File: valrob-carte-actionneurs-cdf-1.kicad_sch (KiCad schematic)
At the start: 57 parts, among them J10 Conn_01x04_Pin, J2 Conn_01x02, J3 USB_C_Receptacle_USB2.0_14P, J4 Conn_01x02, M1 Motor_Servo, U2 SN65HVD230, U3 LDL212PV33R, U5 ESP32-S3FN8, Y1 48M

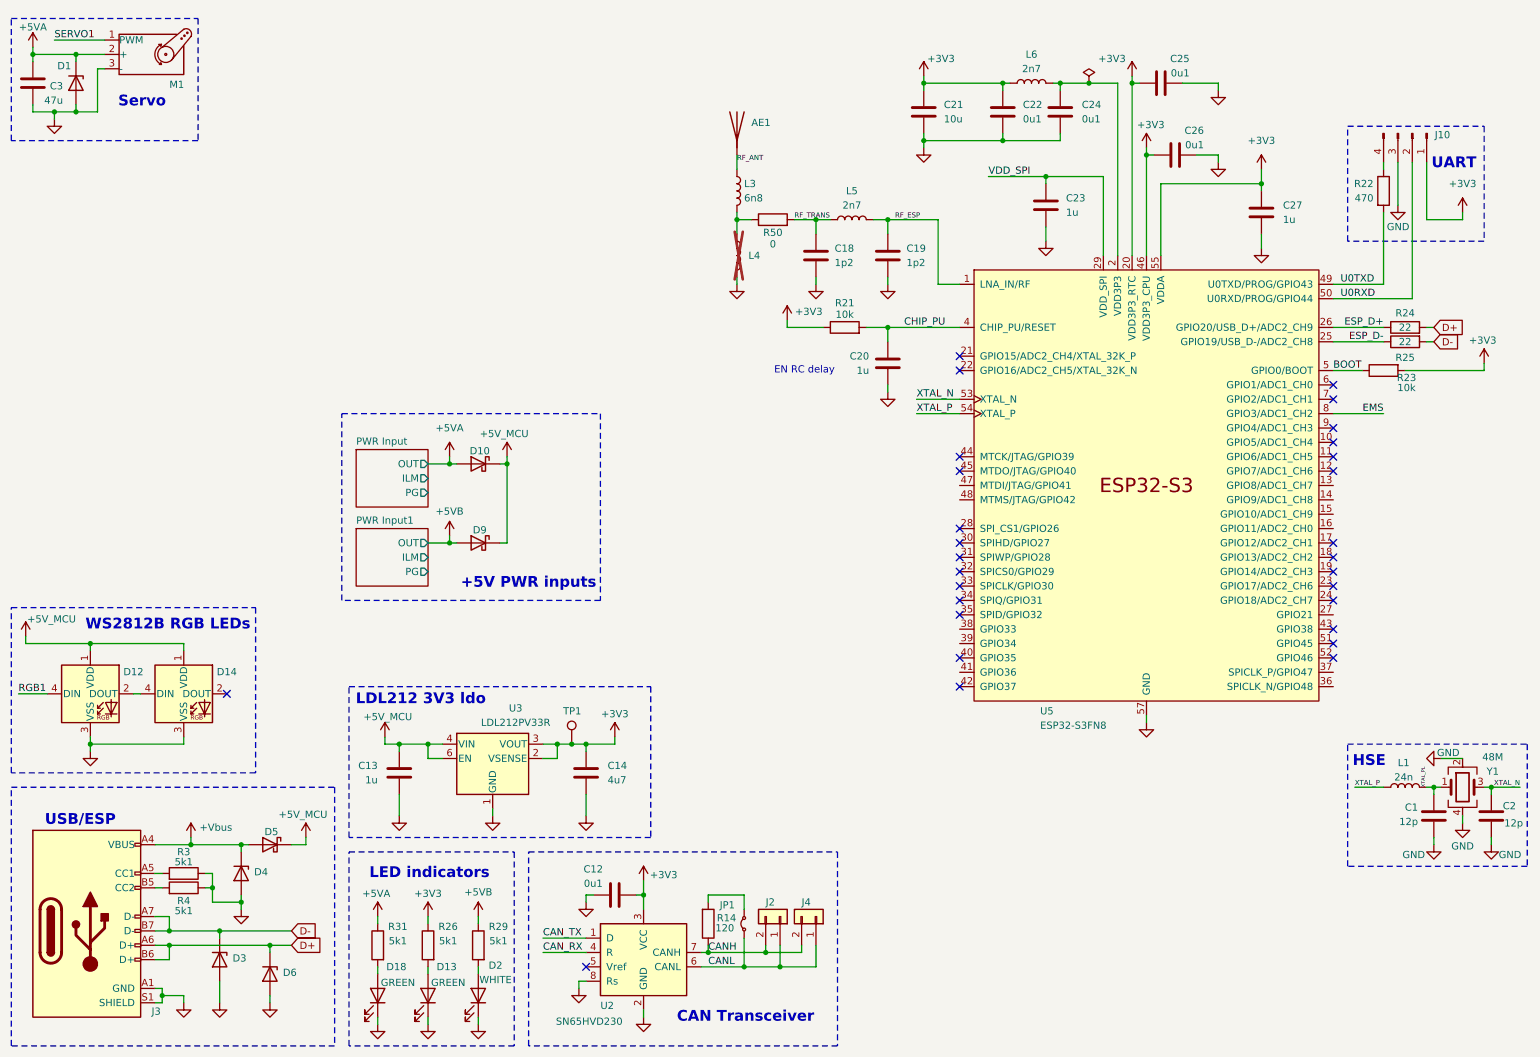
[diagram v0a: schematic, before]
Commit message: schem: connect peripherals gpios
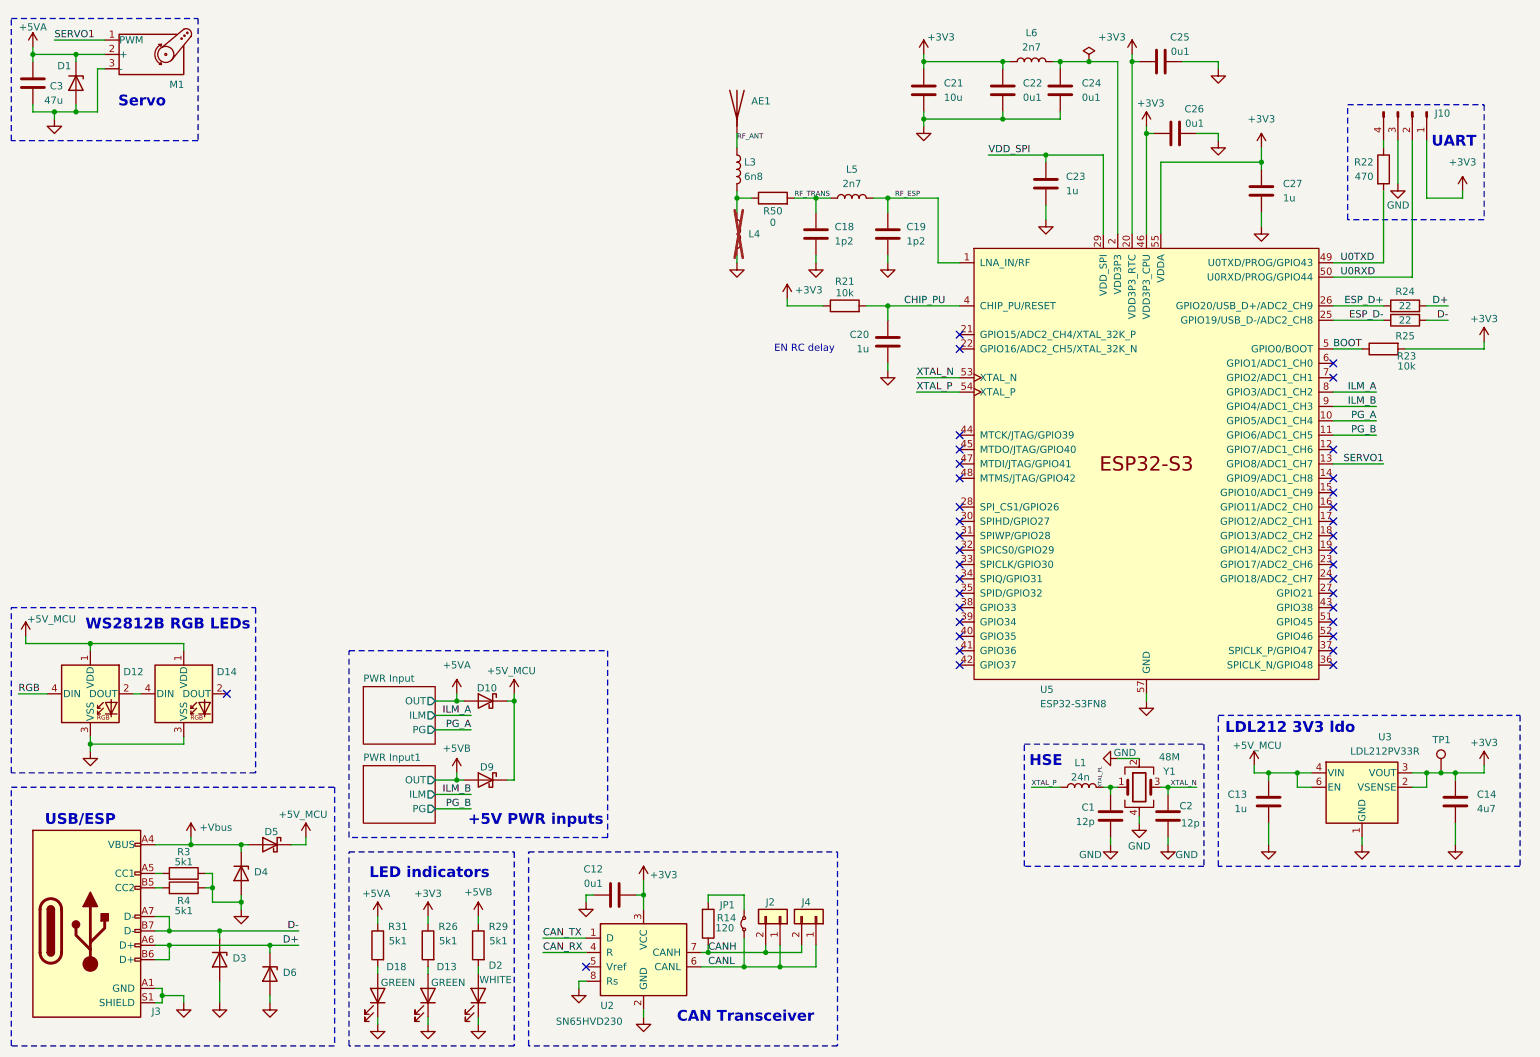
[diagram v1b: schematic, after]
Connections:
- net SERVO1: now also U5.13 (GPIO8/ADC1_CH7)
- net PG_A: now reaches U5.10 (GPIO5/ADC1_CH4)
- net PG_B: now reaches U5.11 (GPIO6/ADC1_CH5)
- net ILM_B: now reaches U5.9 (GPIO4/ADC1_CH3)
- net EMS renamed ILM_A
- net RGB1 renamed RGB
- no-connect marks 29 -> 37
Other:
- moved on the sheet: AE1, C1, C13, C14, C18, C19, C2, C20, C21, C22, C23, C24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

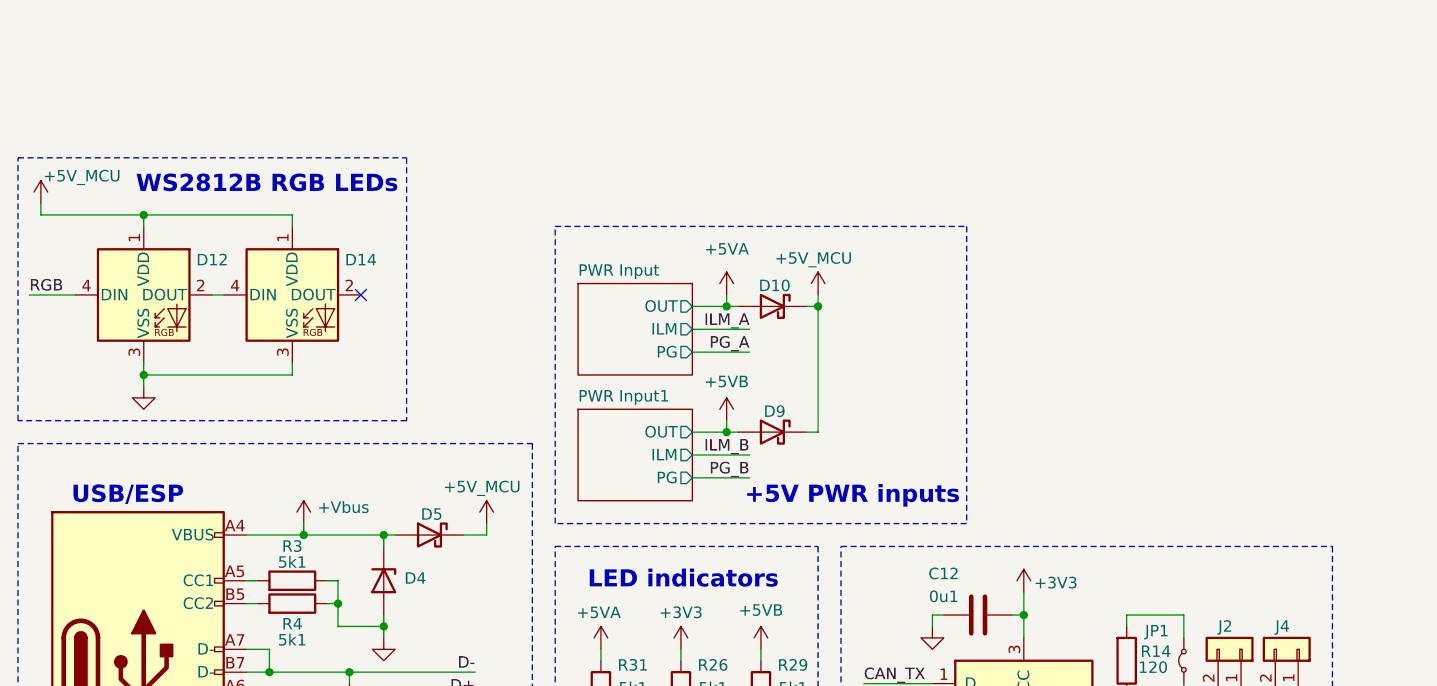
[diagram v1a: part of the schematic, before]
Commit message: schem: add CHIP_PU and BOOT buttons
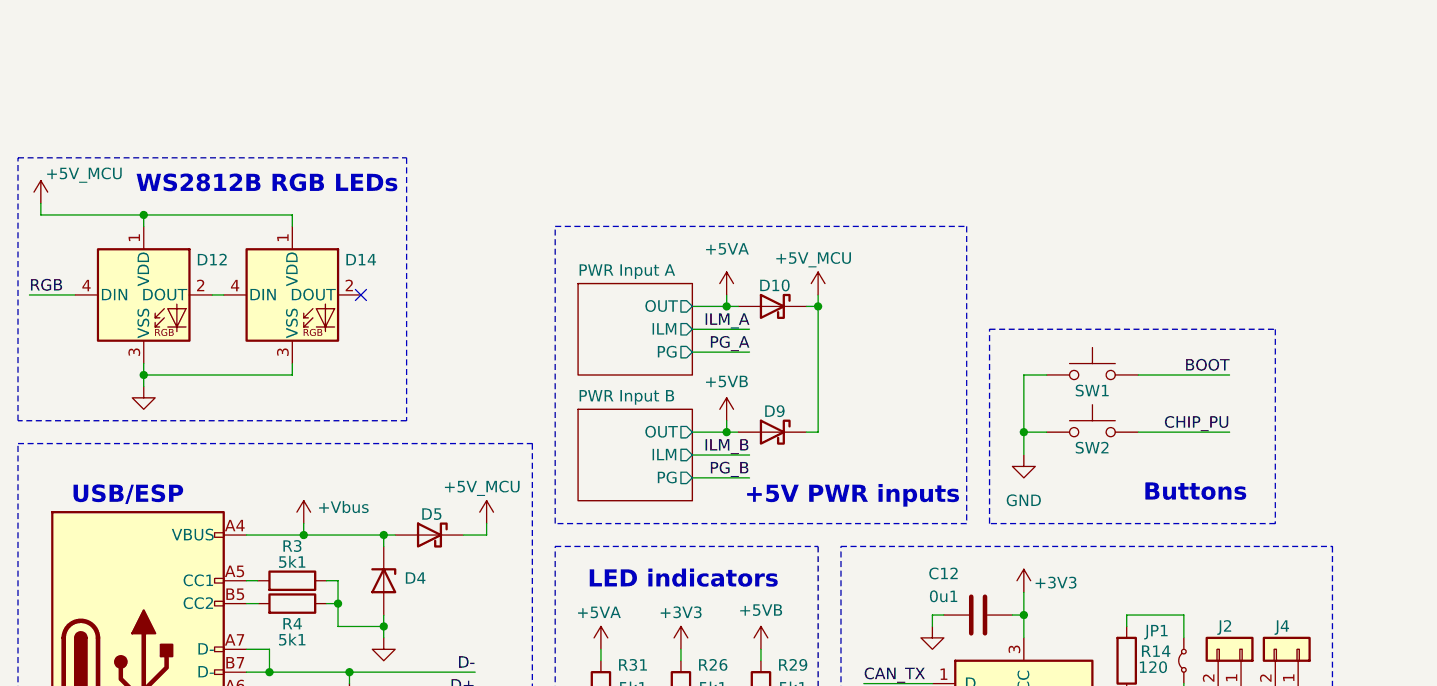
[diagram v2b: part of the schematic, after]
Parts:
- added SW1, SW2: SW_Push, Button_Switch_SMD:SW_SPST_TS-1088-xR020, symbol Switch:SW_Push
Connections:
- net BOOT: now also SW1.2
- net CHIP_PU: now also SW2.2
- net GND: now also SW1.1, SW2.1
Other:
- sheet PWR Input renamed PWR Input A
- sheet PWR Input1 renamed PWR Input B
- note added: "Buttons"

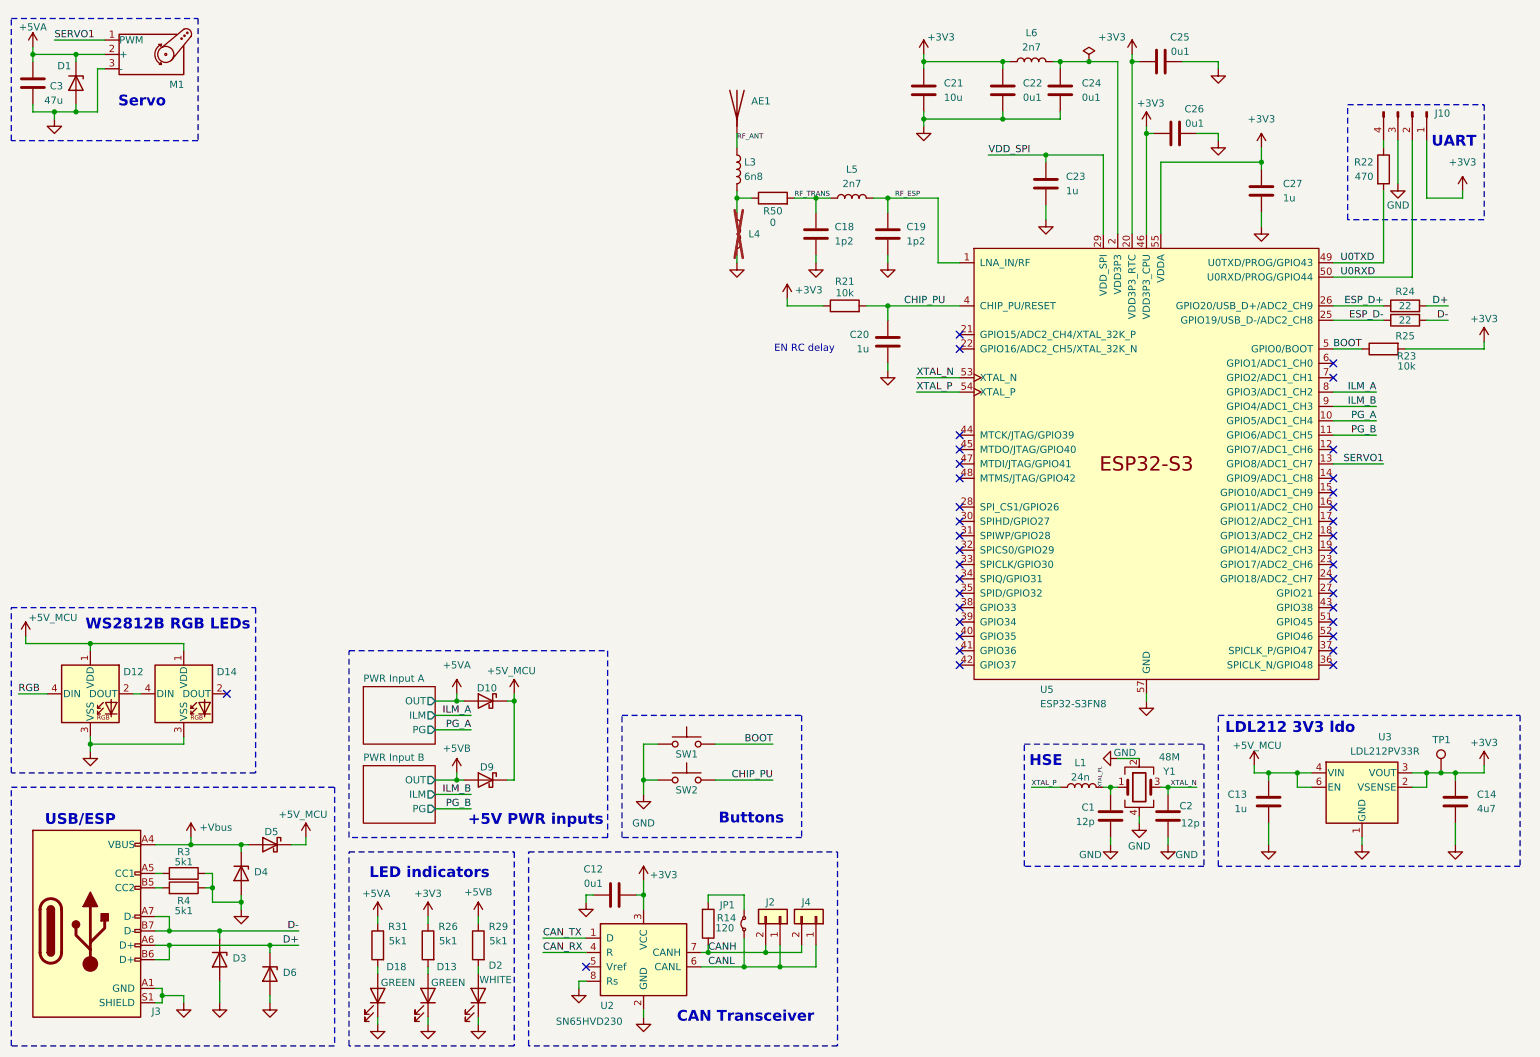
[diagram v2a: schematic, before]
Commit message: schem: add test points
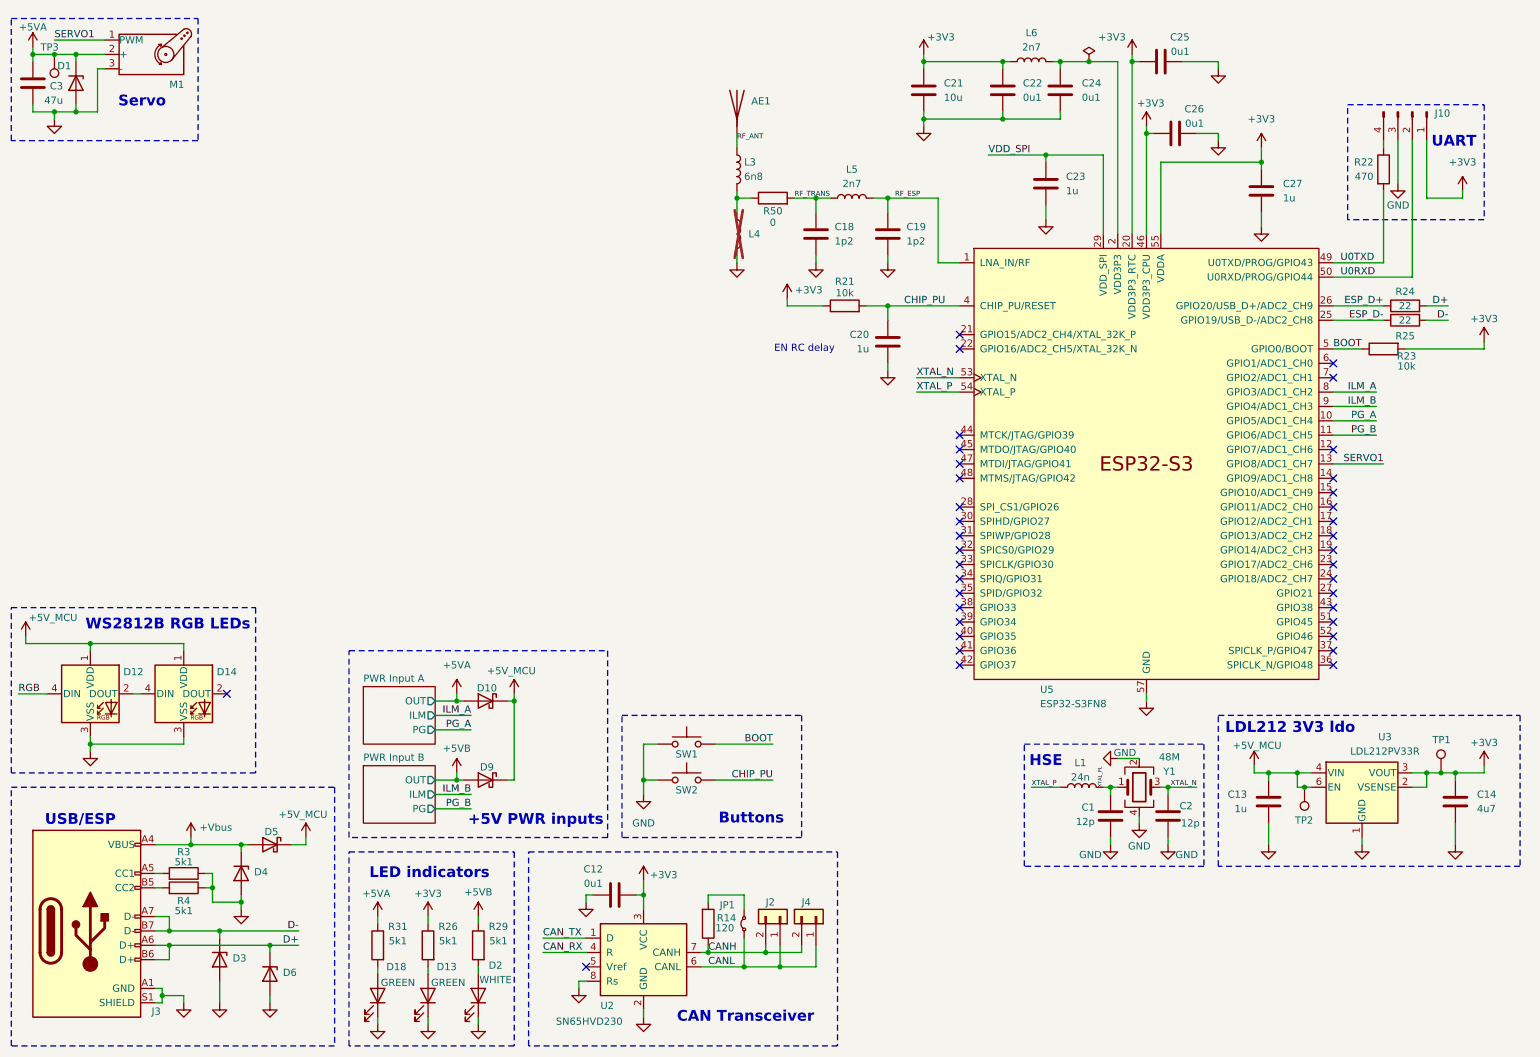
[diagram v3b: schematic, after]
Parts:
- added TP2, TP3: TestPoint, TestPoint:TestPoint_Pad_D2.0mm, symbol Connector:TestPoint
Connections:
- net +5VA: now also TP3.1
- net +5V_MCU: now also TP2.1
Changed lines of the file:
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@@
 	)
 	(junction
+		(at 22.86 20.32)
+		(diameter 0)
+		(color 0 0 0 0)
+	)
+	(junction
 		(at 93.98 148.59)
 		(diameter 0)
@@
 	)
 	(junction
+		(at 243.84 149.86)
+		(diameter 0)
+		(color 0 0 0 0)
+	)
+	(junction
 		(at 170.18 64.77)
 		(diameter 0)
@@
 	(wire
 		(pts
-			(xy 19.05 20.32) (xy 26.67 20.32)
+			(xy 19.05 20.32) (xy 22.86 20.32)
 		)
 		(stroke
@@
 	(wire
 		(pts
+			(xy 22.86 20.32) (xy 26.67 20.32)
+		)
+		(stroke
+			(width 0)
+			(type default)
+		)
+	)
+	(wire
+		(pts
 			(xy 210.82 144.78) (xy 214.63 144.78)
 		)
@@
 	(wire
 		(pts
+			(xy 243.84 149.86) (xy 242.57 149.86)
+		)
+		(stroke
+			(width 0)
+			(type default)
+		)
+	)
+	(wire
+		(pts
 			(xy 170.18 55.88) (xy 170.18 57.15)
 		)
@@
 	(wire
 		(pts
-			(xy 245.11 149.86) (xy 242.57 149.86)
+			(xy 245.11 149.86) (xy 243.84 149.86)
 		)
 		(stroke
@@
 	)
 	(symbol
+		(lib_id "Connector:TestPoint")
+		(at 22.86 20.32 180)
+		(unit 1)
+		(exclude_from_sim no)
+		(in_bom no)
+		(on_board yes)
+		(dnp no)
+		(property "Reference" "TP3"
+			(at 23.622 19.05 0)
+			(effects
+				(font
+					(size 1.27 1.27)
+				)
+				(justify left)
+			)
+		)
+		(property "Value" "TestPoint"
+			(at 20.32 22.3521 0)
+			(effects
+				(font
+					(size 1.27 1.27)
+				)
+				(justify left)
+				(hide yes)
+			)
+		)
+		(property "Footprint" "TestPoint:TestPoint_Pad_D2.0mm"
+			(at 17.78 20.32 0)
+			(effects
+				(font
+					(size 1.27 1.27)
+				)
+				(hide yes)
+			)
+		)
+		(property "Datasheet" "~"
+			(at 17.78 20.32 0)
+			(effects
+				(font
+					(size 1.27 1.27)
+				)
+				(hide yes)
+			)
+		)
+		(property "Description" "test point"
+			(at 22.86 20.32 0)
+			(effects
+				(font
+					(size 1.27 1.27)
+				)
+				(hide yes)
+			)
+		)
+		(pin "1"
+		)
+		(instances
+			(project "valrob-carte-actionneurs-cdf-1"
+				(path "/6d04427e-e45e-4b7f-8323-501f87acc543"
+					(reference "TP3")
+					(unit 1)
+				)
+			)
+		)
+	)
+	(symbol
 		(lib_id "power:GND")
 		(at 60.96 187.96 0)
@@
 					(unit 1)
 				)
+			)
+		)
+	)
+	(symbol
+		(lib_id "Connector:TestPoint")
+		(at 243.84 149.86 180)
+		(unit 1)
+		(exclude_from_sim no)
+		(in_bom no)
+		(on_board yes)
+		(dnp no)
+		(property "Reference" "TP2"
+			(at 245.364 155.702 0)
+			(effects
+				(font
+					(size 1.27 1.27)
+				)
+				(justify left)
+			)
+		)
+		(property "Value" "TestPoint"
+			(at 241.3 151.8921 0)
+			(effects
+				(font
+					(size 1.27 1.27)
+				)
+				(justify left)
+				(hide yes)
+			)
+		)
+		(property "Footprint" "TestPoint:TestPoint_Pad_D2.0mm"
+			(at 238.76 149.86 0)
+			(effects
+				(font
+					(size 1.27 1.27)
+				)
+				(hide yes)
+			)
+		)
+		(property "Datasheet" "~"
+			(at 238.76 149.86 0)
+			(effects
+				(font
+					(size 1.27 1.27)
+				)
+				(hide yes)
+			)
+		)
+		(property "Description" "test point"
+			(at 243.84 149.86 0)
+			(effects
+				(font
+					(size 1.27 1.27)
+				)
+				(hide yes)
+			)
+		)
+		(pin "1"
+		)
+		(instances
+			(project "valrob-carte-actionneurs-cdf-1"
+				(path "/6d04427e-e45e-4b7f-8323-501f87acc543"
+					(reference "TP2")
+					(unit 1)
+				)
